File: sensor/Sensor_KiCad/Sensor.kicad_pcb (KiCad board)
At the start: 2 copper layers, 111 x 57.4 mm, 42 parts, among them U1 LM358, U2 LM358, U3 LM358, U4 LM358, U5 LM358, U6 LM7805_TO220

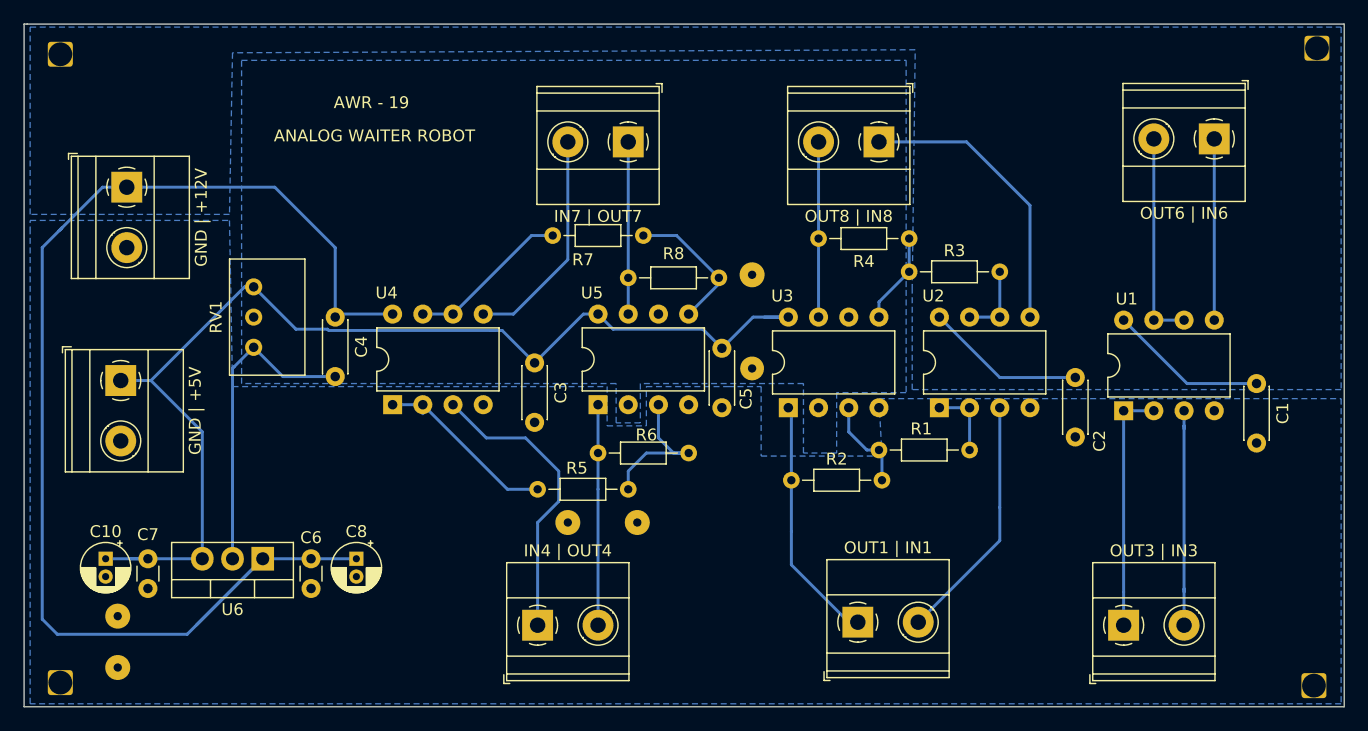
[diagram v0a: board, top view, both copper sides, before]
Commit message: corrected kiCad errors
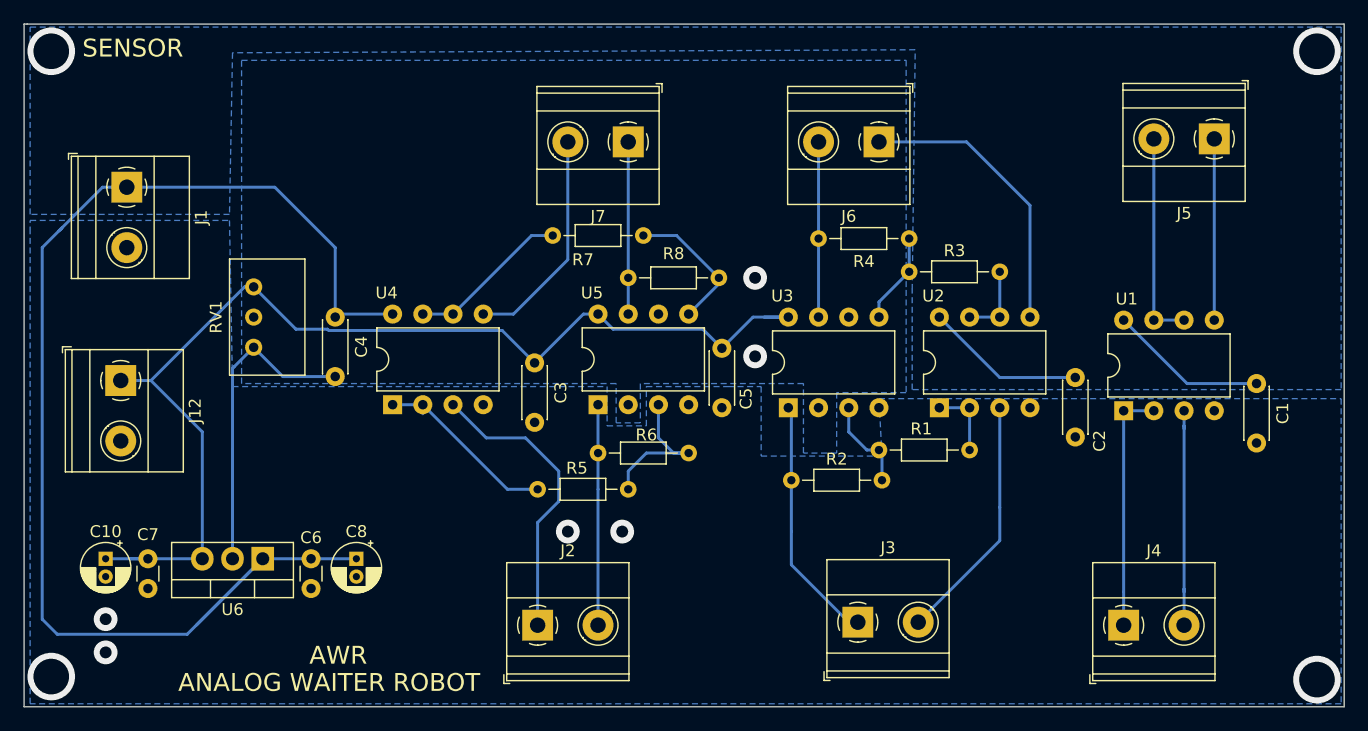
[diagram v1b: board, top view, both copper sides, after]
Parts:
- removed ANALOG WAITER ROBOT: Conn_01x01_Female, Connector_Wire:SolderWire-0.5sqmm_1x01_D0.9mm_OD2.1mm
- removed AWR - 19: Conn_01x01_Female, Connector_Wire:SolderWire-0.5sqmm_1x01_D0.9mm_OD2.1mm
- removed JP1, JP10, JP3, JP4, JP5, JP6, JP8, JP9: Conn_01x01_Female, Connector_Wire:SolderWire-0.5sqmm_1x01_D0.9mm_OD2.1mm
- J1: renamed from GND | +12V 
- J12: renamed from GND | +5V
- J2: renamed from IN4 | OUT4
- J3: renamed from OUT1 | IN1
- J4: renamed from OUT3 | IN3
- J5: renamed from OUT6 | IN6
- J6: renamed from OUT8 | IN8
- J7: renamed from IN7 | OUT7
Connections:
- U1 pad 4: (no net) -> GND
- U1 pad 8: (no net) -> +12V
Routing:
- net (no net): track 0.36 -> 0.00 mm, vias 0 -> 4
- net GND: track 35.6 -> 35.9 mm, vias 0 -> 4
- net VREF: vias 0 -> 2
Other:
- board text added: "ANALOG WAITER ROBOT"
- board text added: "AWR"
- board text added: "SENSOR"

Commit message: update sensor pads and Kicad
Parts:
- GND | +12V: renamed from J1
- GND | +5V: renamed from J12
- IN_4 | OUT_4: renamed from J2
- IN_5 | OUT_5: renamed from J7
- OUT_1 | IN_1: renamed from J3
- OUT_3 | IN_3: renamed from J4
- OUT_6 | IN_6: renamed from J5
- OUT_8 | IN_8: renamed from J6
- moved GND | +12V 0.51 mm to (45.7, 89.9)
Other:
- board text added: "AWR-19_SENSOR"
- board text removed: "ANALOG WAITER ROBOT"
- board text removed: "AWR"
- board text removed: "SENSOR"

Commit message: edited simulations (output/input names)
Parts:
- S1 | SENSOR1: renamed from OUT_1 | IN_1
- S3 | SENSOR3: renamed from OUT_3 | IN_3
- S6 | SENSOR6: renamed from OUT_6 | IN_6
- S8 | SENSOR8: renamed from OUT_8 | IN_8
- SENSOR4 | S4: renamed from IN_4 | OUT_4
- SENSOR5 | S5: renamed from IN_5 | OUT_5
